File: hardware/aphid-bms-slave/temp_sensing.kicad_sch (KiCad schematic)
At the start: 10 parts

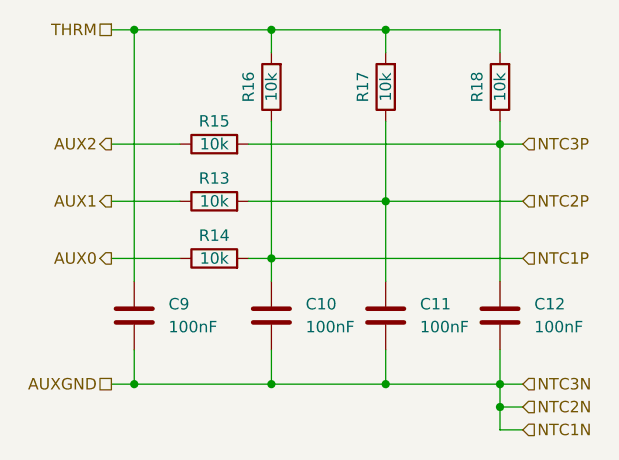
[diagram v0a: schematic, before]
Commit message: Worked on BMS slave schematic and layout
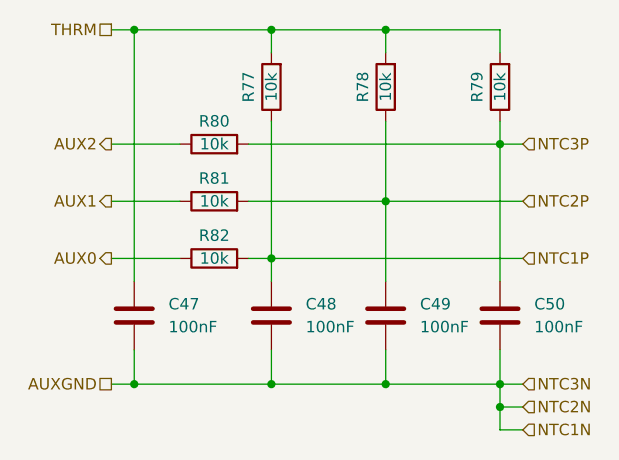
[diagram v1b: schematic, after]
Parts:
- C47: renamed from C9; footprint (none) -> Capacitor_SMD:C_0805_2012Metric
- C48: renamed from C10; footprint (none) -> Capacitor_SMD:C_0805_2012Metric
- C49: renamed from C11; footprint (none) -> Capacitor_SMD:C_0805_2012Metric
- C50: renamed from C12; footprint (none) -> Capacitor_SMD:C_0805_2012Metric
- R77: renamed from R16; footprint (none) -> Resistor_SMD:R_0805_2012Metric
- R78: renamed from R17; footprint (none) -> Resistor_SMD:R_0805_2012Metric
- R79: renamed from R18; footprint (none) -> Resistor_SMD:R_0805_2012Metric
- R80: renamed from R15; footprint (none) -> Resistor_SMD:R_0805_2012Metric
- R81: renamed from R13; footprint (none) -> Resistor_SMD:R_0805_2012Metric
- R82: renamed from R14; footprint (none) -> Resistor_SMD:R_0805_2012Metric
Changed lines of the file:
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@@
 		(dnp no)
 		(fields_autoplaced yes)
-		(property "Reference" "C9"
+		(property "Reference" "C47"
 			(at 121.92 87.6299 0)
 			(effects
@@
 			)
 		)
-		(property "Footprint" ""
+		(property "Footprint" "Capacitor_SMD:C_0805_2012Metric"
 			(at 119.0752 92.71 0)
 			(effects
@@
 			(project ""
 				(path "/36f5197f-5a2b-49d7-95ca-bb7937adb059/6ad10743-f962-4727-a803-7895515f10ae"
-					(reference "C9")
+					(reference "C47")
 					(unit 1)
 				)
@@
 		(dnp no)
 		(fields_autoplaced yes)
-		(property "Reference" "C10"
+		(property "Reference" "C48"
 			(at 137.16 87.6299 0)
 			(effects
@@
 			)
 		)
-		(property "Footprint" ""
+		(property "Footprint" "Capacitor_SMD:C_0805_2012Metric"
 			(at 134.3152 92.71 0)
 			(effects
@@
 			(project "aphid-bms-slave"
 				(path "/36f5197f-5a2b-49d7-95ca-bb7937adb059/6ad10743-f962-4727-a803-7895515f10ae"
-					(reference "C10")
+					(reference "C48")
 					(unit 1)
 				)
@@
 		(on_board yes)
 		(dnp no)
-		(property "Reference" "R13"
+		(property "Reference" "R81"
 			(at 127 73.66 90)
 			(effects
@@
 			)
 		)
-		(property "Footprint" ""
+		(property "Footprint" "Resistor_SMD:R_0805_2012Metric"
 			(at 127 77.978 90)
 			(effects
@@
 			(project ""
 				(path "/36f5197f-5a2b-49d7-95ca-bb7937adb059/6ad10743-f962-4727-a803-7895515f10ae"
-					(reference "R13")
+					(reference "R81")
 					(unit 1)
 				)
@@
 		(on_board yes)
 		(dnp no)
-		(property "Reference" "R17"
+		(property "Reference" "R78"
 			(at 143.51 63.5 90)
 			(effects
@@
 			)
 		)
-		(property "Footprint" ""
+		(property "Footprint" "Resistor_SMD:R_0805_2012Metric"
 			(at 147.828 63.5 90)
 			(effects
@@
 			(project "aphid-bms-slave"
 				(path "/36f5197f-5a2b-49d7-95ca-bb7937adb059/6ad10743-f962-4727-a803-7895515f10ae"
-					(reference "R17")
+					(reference "R78")
 					(unit 1)
 				)
@@
 		(on_board yes)
 		(dnp no)
-		(property "Reference" "R14"
+		(property "Reference" "R82"
 			(at 127 80.01 90)
 			(effects
@@
 			)
 		)
-		(property "Footprint" ""
+		(property "Footprint" "Resistor_SMD:R_0805_2012Metric"
 			(at 127 84.328 90)
 			(effects
@@
 			(project "aphid-bms-slave"
 				(path "/36f5197f-5a2b-49d7-95ca-bb7937adb059/6ad10743-f962-4727-a803-7895515f10ae"
-					(reference "R14")
+					(reference "R82")
 					(unit 1)
 				)
@@
 		(on_board yes)
 		(dnp no)
-		(property "Reference" "R18"
+		(property "Reference" "R79"
 			(at 156.21 63.5 90)
 			(effects
@@
 			)
 		)
-		(property "Footprint" ""
+		(property "Footprint" "Resistor_SMD:R_0805_2012Metric"
 			(at 160.528 63.5 90)
 			(effects
@@
 			(project "aphid-bms-slave"
 				(path "/36f5197f-5a2b-49d7-95ca-bb7937adb059/6ad10743-f962-4727-a803-7895515f10ae"
-					(reference "R18")
+					(reference "R79")
 					(unit 1)
 				)
@@
 		(dnp no)
 		(fields_autoplaced yes)
-		(property "Reference" "C12"
+		(property "Reference" "C50"
 			(at 162.56 87.6299 0)
 			(effects
@@
 			)
 		)
-		(property "Footprint" ""
+		(property "Footprint" "Capacitor_SMD:C_0805_2012Metric"
 			(at 159.7152 92.71 0)
 			(effects
@@
 			(project "aphid-bms-slave"
 				(path "/36f5197f-5a2b-49d7-95ca-bb7937adb059/6ad10743-f962-4727-a803-7895515f10ae"
-					(reference "C12")
+					(reference "C50")
 					(unit 1)
 				)
@@
 		(on_board yes)
 		(dnp no)
-		(property "Reference" "R15"
+		(property "Reference" "R80"
 			(at 127 67.31 90)
 			(effects
@@
 			)
 		)
-		(property "Footprint" ""
+		(property "Footprint" "Resistor_SMD:R_0805_2012Metric"
 			(at 127 71.628 90)
 			(effects
@@
 			(project "aphid-bms-slave"
 				(path "/36f5197f-5a2b-49d7-95ca-bb7937adb059/6ad10743-f962-4727-a803-7895515f10ae"
-					(reference "R15")
+					(reference "R80")
 					(unit 1)
 				)
@@
 		(on_board yes)
 		(dnp no)
-		(property "Reference" "R16"
+		(property "Reference" "R77"
 			(at 130.81 63.5 90)
 			(effects
@@
 			)
 		)
-		(property "Footprint" ""
+		(property "Footprint" "Resistor_SMD:R_0805_2012Metric"
 			(at 135.128 63.5 90)
 			(effects
@@
 			(project "aphid-bms-slave"
 				(path "/36f5197f-5a2b-49d7-95ca-bb7937adb059/6ad10743-f962-4727-a803-7895515f10ae"
-					(reference "R16")
+					(reference "R77")
 					(unit 1)
 				)
@@
 		(dnp no)
 		(fields_autoplaced yes)
-		(property "Reference" "C11"
+		(property "Reference" "C49"
 			(at 149.86 87.6299 0)
 			(effects
@@
 			)
 		)
-		(property "Footprint" ""
+		(property "Footprint" "Capacitor_SMD:C_0805_2012Metric"
 			(at 147.0152 92.71 0)
 			(effects
@@
 			(project "aphid-bms-slave"
 				(path "/36f5197f-5a2b-49d7-95ca-bb7937adb059/6ad10743-f962-4727-a803-7895515f10ae"
-					(reference "C11")
-					(unit 1)
-				)
+					(reference "C49")
+					(unit 1)
+				)

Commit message: Worked on BMS slave schematic and layout
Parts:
- C47: footprint Capacitor_SMD:C_0805_2012Metric -> Capacitor_SMD:C_0603_1608Metric
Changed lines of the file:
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@@
 			)
 		)
-		(property "Footprint" "Capacitor_SMD:C_0805_2012Metric"
+		(property "Footprint" "Capacitor_SMD:C_0603_1608Metric"
 			(at 119.0752 92.71 0)
 			(effects

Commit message: BMS slave 1.0 done
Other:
- company: (none) -> https://aphid-ev.se
- title: (none) -> aphid-ev BMS slave
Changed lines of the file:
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@@
 	(generator_version "8.0")
 	(paper "A4")
+	(title_block
+		(title "aphid-ev BMS slave")
+		(date "2024-07-23")
+		(rev "1.0")
+		(company "https://aphid-ev.se")
+	)
 	(junction
 		(at 158.75 69.85)
